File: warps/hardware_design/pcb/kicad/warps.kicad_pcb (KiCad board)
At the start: 2 copper layers, 48.9 x 106.7 mm, 127 parts, among them IC1 LM1117-3.3, IC2 LM4040B10, IC3 MCP6004, IC4 STM32F405RGT6, IC5 WM8731, IC6 TL072, J1 PJ301_THONKICONN6, J2 PJ301_THONKICONN6, J3 PJ301_THONKICONN6, J4 PJ301_THONKICONN6, J5 PJ301_THONKICONN6, J6 PJ301_THONKICONN6, J7 PJ301_THONKICONN6, J8 PJ301_THONKICONN6, Q1 8MHz, Q2 12.288MHz

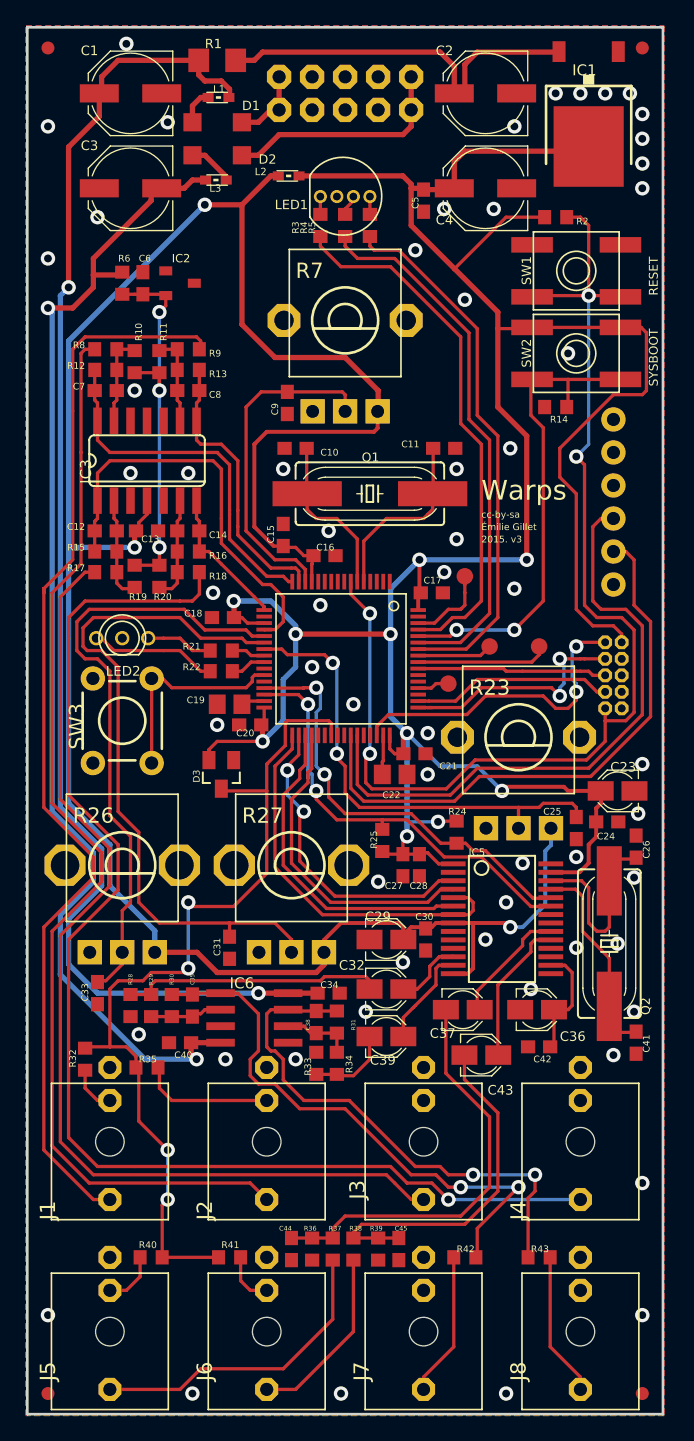
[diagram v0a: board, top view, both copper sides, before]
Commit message: warps caps + wm8731
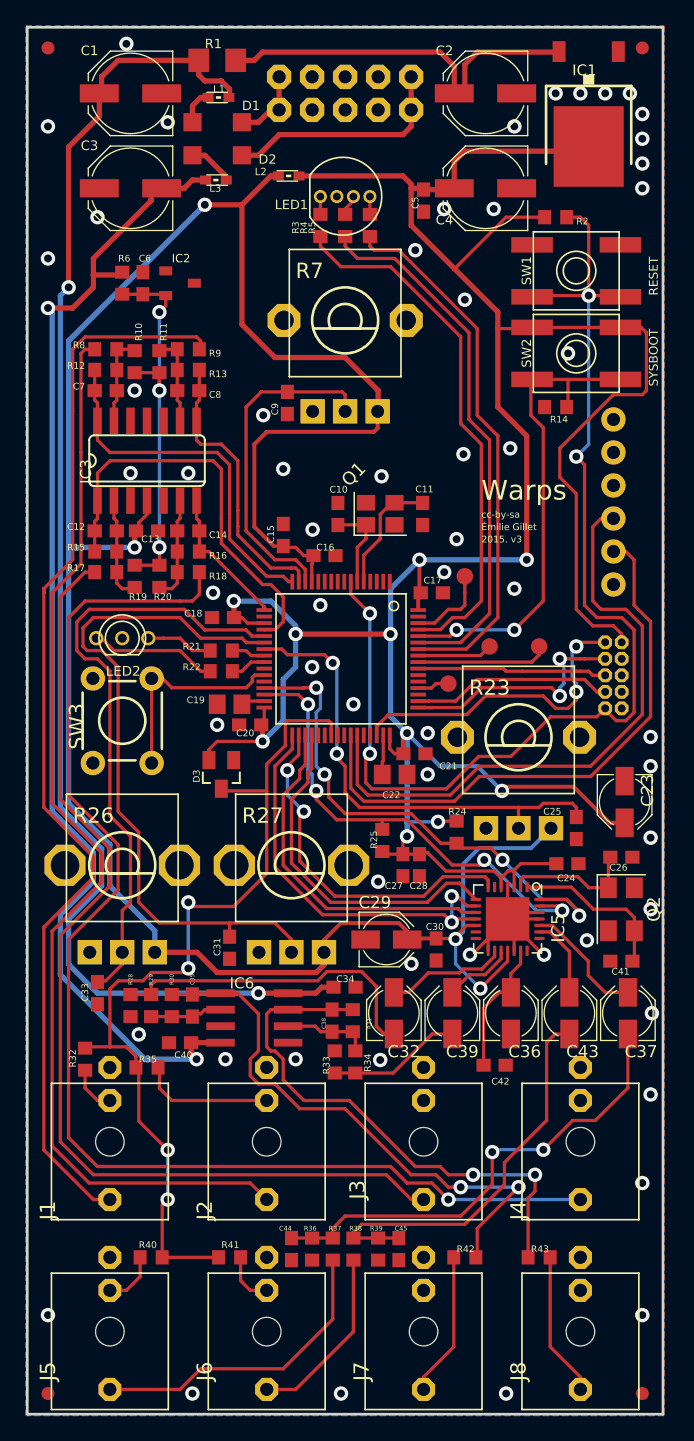
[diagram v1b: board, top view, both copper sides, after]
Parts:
- removed U$2: , warps:ROHS_BIG
- C23, C29, C32, C36, C37, C39, C43: footprint warps:PANASONIC_A -> plaits:PANASONIC_B
- IC5: footprint warps:SSOP28 -> Package_DFN_QFN:QFN-28-1EP_5x5mm_P0.5mm_EP3.35x3.35mm
- JP2: value (none) -> M06SIP
- L1, L2, L3: value (none) -> WE-CBF_0603
- Q1: footprint warps:HC49UP -> Crystal:Crystal_SMD_3225-4Pin_3.2x2.5mm
- Q2: footprint warps:HC49UP -> Crystal:Crystal_SMD_5032-4Pin_5.0x3.2mm
- SW1, SW2: value (none) -> EVQQ2
- SW3: value (none) -> TAC_SWITCHPTH
- moved C37 12.7 mm to (170.2, 127.5), turned to 90 degrees
- moved C43 7.50 mm to (165.8, 127.5), turned to 90 degrees
- moved C41 6.37 mm to (169.8, 123.5), turned to 0 degrees
- moved C10 6.01 mm to (147.9, 89.1), turned to -90 degrees
- moved C39 5.38 mm to (156.8, 127.5), turned to 90 degrees
- moved C11 5.32 mm to (154.5, 89.1), turned to 90 degrees
- moved C24 4.44 mm to (165.6, 116.0)
- moved C42 3.70 mm to (160.0, 131.5), turned to 0 degrees
- moved Q2 2.81 mm to (169.8, 119.5)
- moved C36 2.03 mm to (161.2, 127.5), turned to 90 degrees
- moved C32 1.95 mm to (152.2, 127.5), turned to 90 degrees
- moved Q1 1.73 mm to (151.2, 89.1)
- moved R34 1.43 mm to (149.3, 131.2)
- moved R33 1.43 mm to (147.7, 131.2)
- moved C26 1.40 mm to (169.8, 115.5), turned to 180 degrees
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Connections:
- net ALGORITHM_POT renamed /warps_2/ALGORITHM_POT
- net BOOT_FLASH renamed /warps_2/BOOT_FLASH
- net JTCK renamed /warps_2/JTCK
- net JTDI renamed /warps_2/JTDI
- net JTDO renamed /warps_2/JTDO
- net JTMS renamed /warps_2/JTMS
- net LED_B renamed /warps_2/LED_B
- net LED_CARRIER_G renamed /warps_2/LED_CARRIER_G
- net LED_CARRIER_R renamed /warps_2/LED_CARRIER_R
- net LED_G renamed /warps_2/LED_G
- net LED_R renamed /warps_2/LED_R
- net LEVEL_1_POT renamed /warps_2/LEVEL_1_POT
- net LEVEL_2_POT renamed /warps_2/LEVEL_2_POT
- net PARAMETER_POT renamed /warps_2/PARAMETER_POT
- net RESET renamed /warps_2/RESET
- net RX renamed /warps_2/RX
- net SW_CARRIER renamed /warps_2/SW_CARRIER
- net TX renamed /warps_2/TX
- C11 pad 2: N$7 -> Net-(C11-Pad2)
- C26 pad 2: N$41 -> Net-(C26-Pad2)
- C36 pad +: N$17 -> Net-(C36-Pad+)
- C41 pad 2: N$40 -> Net-(C41-Pad2)
- C42 pad 1: N$17 -> Net-(C36-Pad+)
- D3 pad 3: NORMALIZATION_PROBE -> unconnected-(D3-Pad3)
- IC4 pad 10: (no net) -> unconnected-(IC4-Pad10)
- IC4 pad 11: (no net) -> unconnected-(IC4-Pad11)
- IC4 pad 2: (no net) -> unconnected-(IC4-Pad2)
- IC4 pad 29: I2C_SCL -> /warps_2/I2C_SCL
- IC4 pad 3: (no net) -> unconnected-(IC4-Pad3)
- IC4 pad 30: I2C_SDA -> /warps_2/I2C_SDA
- IC4 pad 33: I2S_LRCK -> /warps_2/I2S_LRCK
- IC4 pad 34: I2S_SCK -> /warps_2/I2S_SCK
- IC4 pad 35: I2S_SIN -> /warps_2/I2S_SIN
- IC4 pad 36: I2S_SOUT -> /warps_2/I2S_SOUT
- IC4 pad 37: (no net) -> unconnected-(IC4-Pad37)
- IC4 pad 38: (no net) -> unconnected-(IC4-Pad38)
- IC4 pad 4: (no net) -> unconnected-(IC4-Pad4)
- IC4 pad 40: (no net) -> unconnected-(IC4-Pad40)
- IC4 pad 41: (no net) -> unconnected-(IC4-Pad41)
- IC4 pad 44: (no net) -> unconnected-(IC4-Pad44)
- IC4 pad 45: (no net) -> unconnected-(IC4-Pad45)
- IC4 pad 5: N$7 -> Net-(C11-Pad2)
- IC4 pad 51: (no net) -> unconnected-(IC4-Pad51)
- IC4 pad 53: (no net) -> unconnected-(IC4-Pad53)
- IC4 pad 54: (no net) -> unconnected-(IC4-Pad54)
- IC4 pad 8: (no net) -> unconnected-(IC4-Pad8)
- IC4 pad 9: (no net) -> unconnected-(IC4-Pad9)
- IC5 pad 1: +3V3 -> Net-(C41-Pad2)
- IC5 pad 10: (no net) -> /warps_2/I2S_SIN
- IC5 pad 11: GND -> /warps_2/I2S_LRCK
- IC5 pad 12: MOD_OUT -> +3V3_A
- IC5 pad 13: AUX_OUT -> unconnected-(IC5-Pad13)
- IC5 pad 14: +3V3_A -> unconnected-(IC5-Pad14)
- IC5 pad 16: N$17 -> MOD_OUT
- IC5 pad 17: (no net) -> AUX_OUT
- IC5 pad 18: (no net) -> +3V3_A
- IC5 pad 19: IN_2 -> GND
- IC5 pad 2: (no net) -> Net-(C26-Pad2)
- IC5 pad 20: IN_1 -> Net-(C36-Pad+)
- IC5 pad 21: GND -> unconnected-(IC5-Pad21)
- IC5 pad 22: GND -> unconnected-(IC5-Pad22)
- IC5 pad 23: I2C_SDA -> IN_2
- IC5 pad 24: I2C_SCL -> IN_1
- IC5 pad 25: N$40 -> GND
- IC5 pad 26: N$41 -> GND
- IC5 pad 27: +3V3 -> /warps_2/I2C_SDA
- IC5 pad 28: GND -> /warps_2/I2C_SCL
- IC5 pad 3: I2S_SCK -> +3V3
- IC5 pad 4: I2S_SOUT -> GND
- IC5 pad 5: I2S_LRCK -> +3V3
- IC5 pad 6: I2S_SIN -> unconnected-(IC5-Pad6)
- IC5 pad 7: I2S_LRCK -> /warps_2/I2S_SCK
- IC5 pad 8: +3V3_A -> /warps_2/I2S_SOUT
- IC5 pad 9: (no net) -> /warps_2/I2S_LRCK
- J3 pad P2: (no net) -> unconnected-(J3-PadP2)
- J4 pad P2: (no net) -> unconnected-(J4-PadP2)
- J7 pad P2: (no net) -> unconnected-(J7-PadP2)
- J8 pad P2: (no net) -> unconnected-(J8-PadP2)
- JP1 pad 7: (no net) -> unconnected-(JP1-Pad7)
- JP2 pad 2: (no net) -> unconnected-(JP2-Pad2)
- JP2 pad 3: (no net) -> unconnected-(JP2-Pad3)
- JP2 pad 6: (no net) -> unconnected-(JP2-Pad6)
- Q1 pad 2: N$7 -> GND
- Q2 pad 1: N$41 -> Net-(C26-Pad2)
- Q2 pad 2: N$40 -> GND
- R24 pad 1: I2C_SCL -> /warps_2/I2C_SCL
- R25 pad 1: I2C_SDA -> /warps_2/I2C_SDA
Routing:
- net /warps_2/I2C_SCL: track 0.00 -> 40.1 mm, vias 0 -> 4
- net /warps_2/I2C_SDA: track 0.00 -> 37.3 mm, vias 0 -> 4
- net I2C_SDA: track 34.1 -> 0.00 mm, vias 2 -> 0
- net I2C_SCL: track 33.4 -> 0.00 mm, vias 2 -> 0
- net /warps_2/I2S_LRCK: track 0.00 -> 32.2 mm, vias 0 -> 2
- net I2S_LRCK: track 29.9 -> 0.00 mm
- net /warps_2/I2S_SCK: track 0.00 -> 27.6 mm, vias 0 -> 2
- net /warps_2/I2S_SOUT: track 0.00 -> 27.0 mm
- net /warps_2/I2S_SIN: track 0.00 -> 27.0 mm
- net I2S_SIN: track 25.3 -> 0.00 mm
- net I2S_SOUT: track 24.7 -> 0.00 mm
- net I2S_SCK: track 24.1 -> 0.00 mm, vias 2 -> 0
- net GND: track 0.00 -> 21.5 mm, vias 60 -> 59
- net N$40: track 16.1 -> 0.00 mm
- net N$41: track 15.2 -> 0.00 mm
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
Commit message: warps cleanup tracks and vias
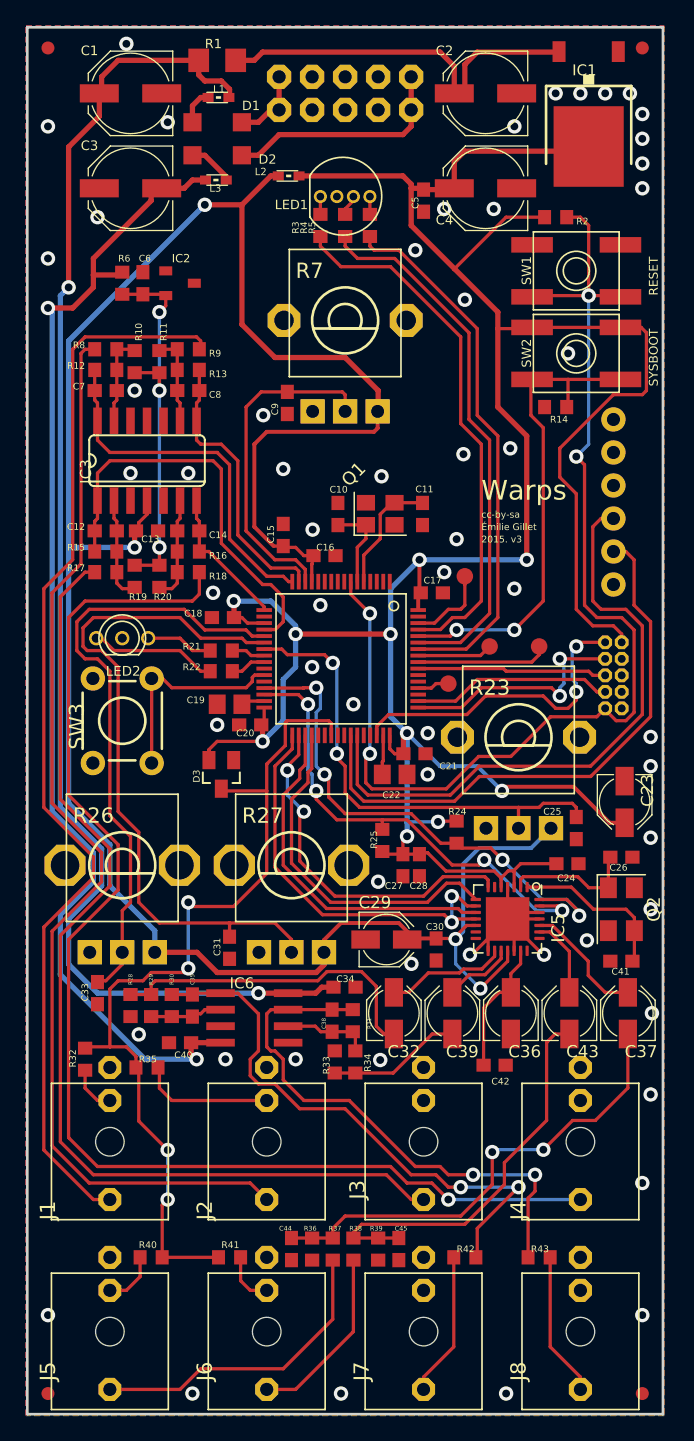
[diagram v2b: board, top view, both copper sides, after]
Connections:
- D3 pad 3: unconnected-(D3-Pad3) -> NORMALIZATION_PROBE
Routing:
- net GND: track 21.5 -> 17.7 mm
- net +3V3: track 224.5 -> 222.2 mm
- net VEE: track 91.0 -> 89.9 mm
- net NORMALIZATION_PROBE: track 69.3 -> 68.3 mm
- net Net-(C2-Pad+): track 30.3 -> 29.4 mm
- net +3V3_A: track 180.4 -> 179.6 mm
- net Net-(J1-PadP3): track 84.0 -> 83.2 mm
- net Net-(C38-Pad1): track 7.13 -> 6.42 mm
- net Net-(D1-PadA): track 5.80 -> 5.16 mm
- net /warps_2/I2C_SDA: track 37.3 -> 36.7 mm
- net Net-(D2-PadC): track 17.8 -> 17.1 mm
- net /warps_2/I2C_SCL: track 40.1 -> 39.5 mm
- net /warps_2/RESET: track 90.1 -> 89.6 mm

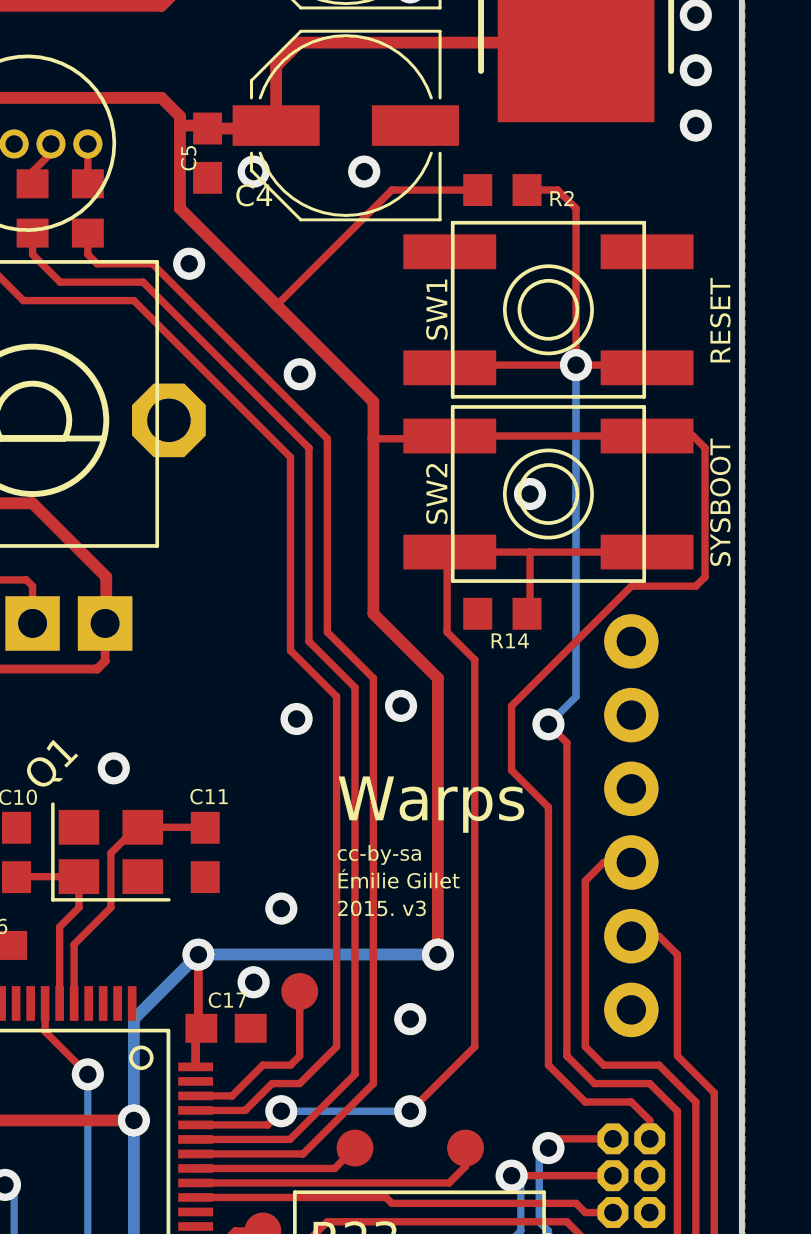
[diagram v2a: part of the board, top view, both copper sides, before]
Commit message: warps SMD boot/reset buttons
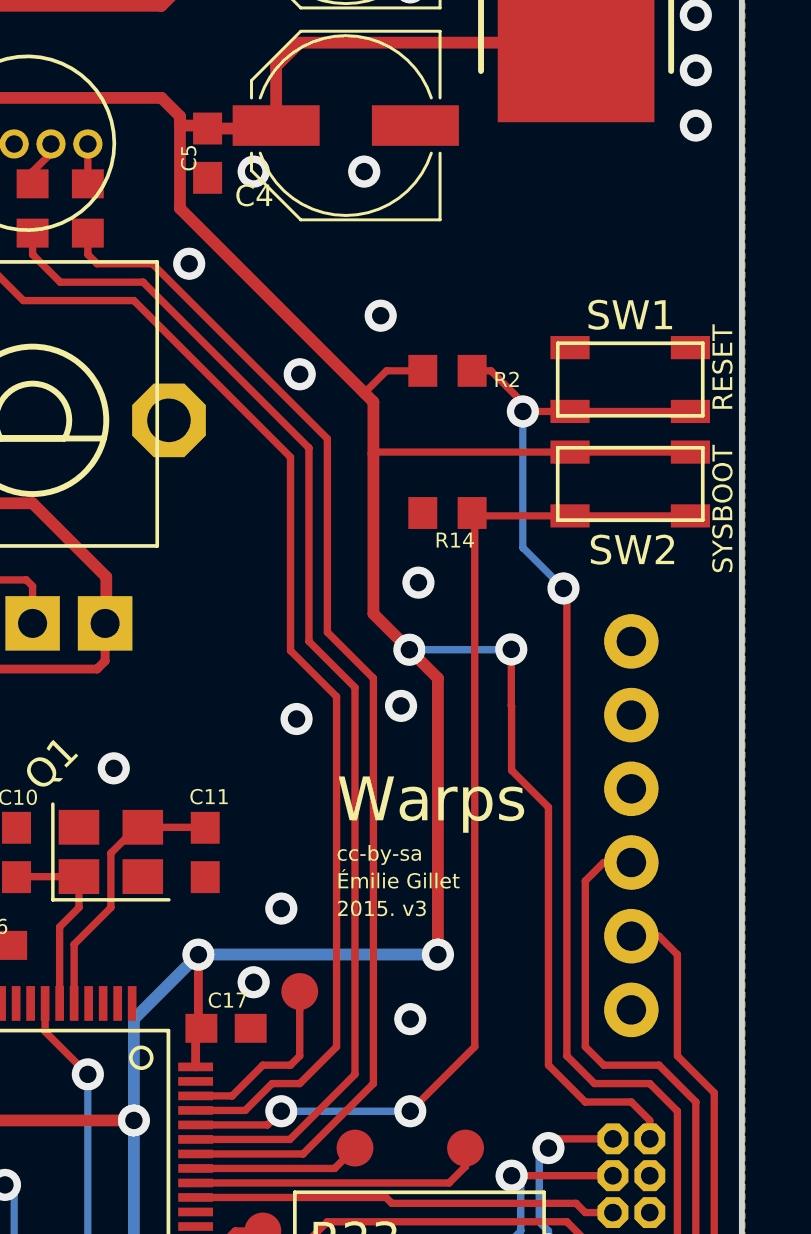
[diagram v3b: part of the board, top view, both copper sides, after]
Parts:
- SW1, SW2: footprint warps:EVQ-Q2 -> Supercell 1.3:k2-1808 pushbutton switch
- moved R2 6.51 mm to (162.8, 72.5)
- moved R14 3.96 mm to (162.8, 77.4)
- moved SW1 3.70 mm to (169.1, 72.8)
- moved SW2 2.84 mm to (169.1, 76.4)
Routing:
- net +3V3: track 222.2 -> 207.9 mm, vias 10 -> 12
- net /warps_2/RESET: track 89.6 -> 82.3 mm
- net GND: vias 59 -> 60
